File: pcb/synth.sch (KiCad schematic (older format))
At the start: 48 parts, among them J1 Conn_01x06, SW1 SW_Push, SW10 SW_Push, SW11 SW_Push, SW12 SW_Push, SW13 SW_Push, SW14 SW_Push, SW15 SW_Push, SW16 SW_Push, SW17 SW_Push, SW18 SW_Push, SW19 SW_Push, SW2 SW_Push, SW20 SW_Push, SW21 SW_Push, SW22 SW_Push, SW23 SW_Push, SW24 SW_Push, SW3 SW_Push, SW4 SW_Push, SW5 SW_Push, SW6 SW_Push, SW7 SW_Push, SW8 SW_Push, SW9 SW_Push, U1 STM32F407VGTx, Y1 Crystal

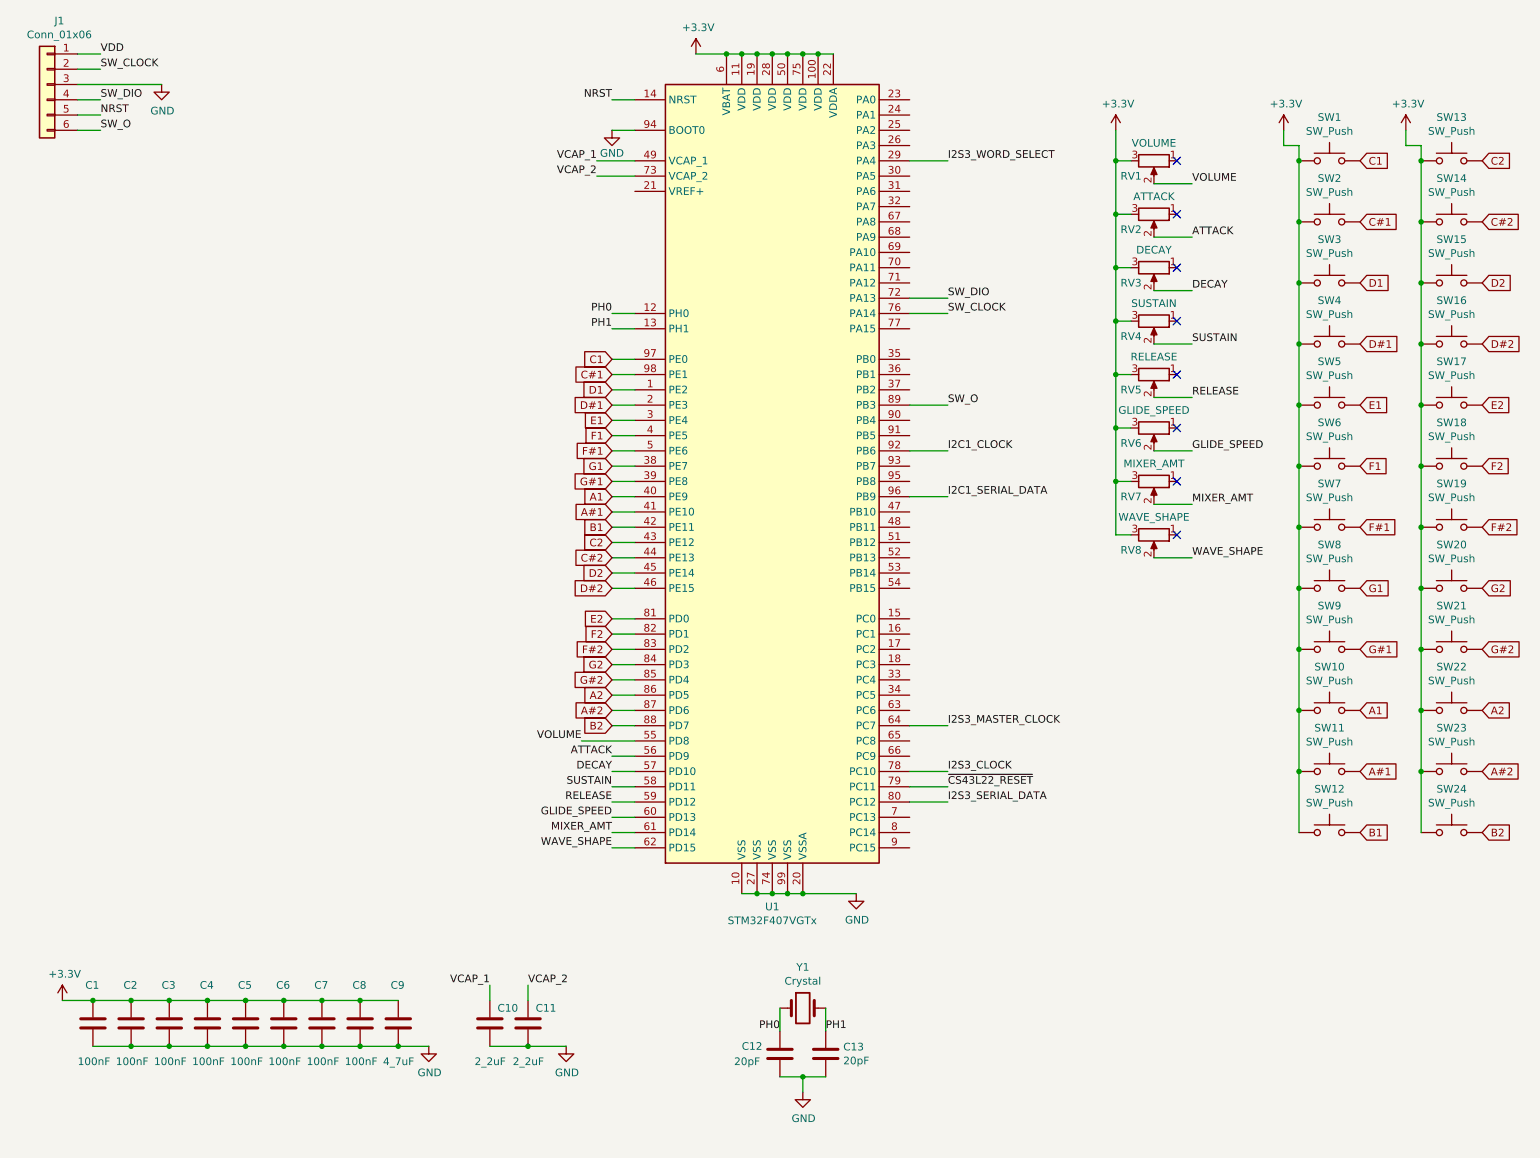
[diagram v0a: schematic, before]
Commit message: Add power flags and update the crystal to be 8 MHz.
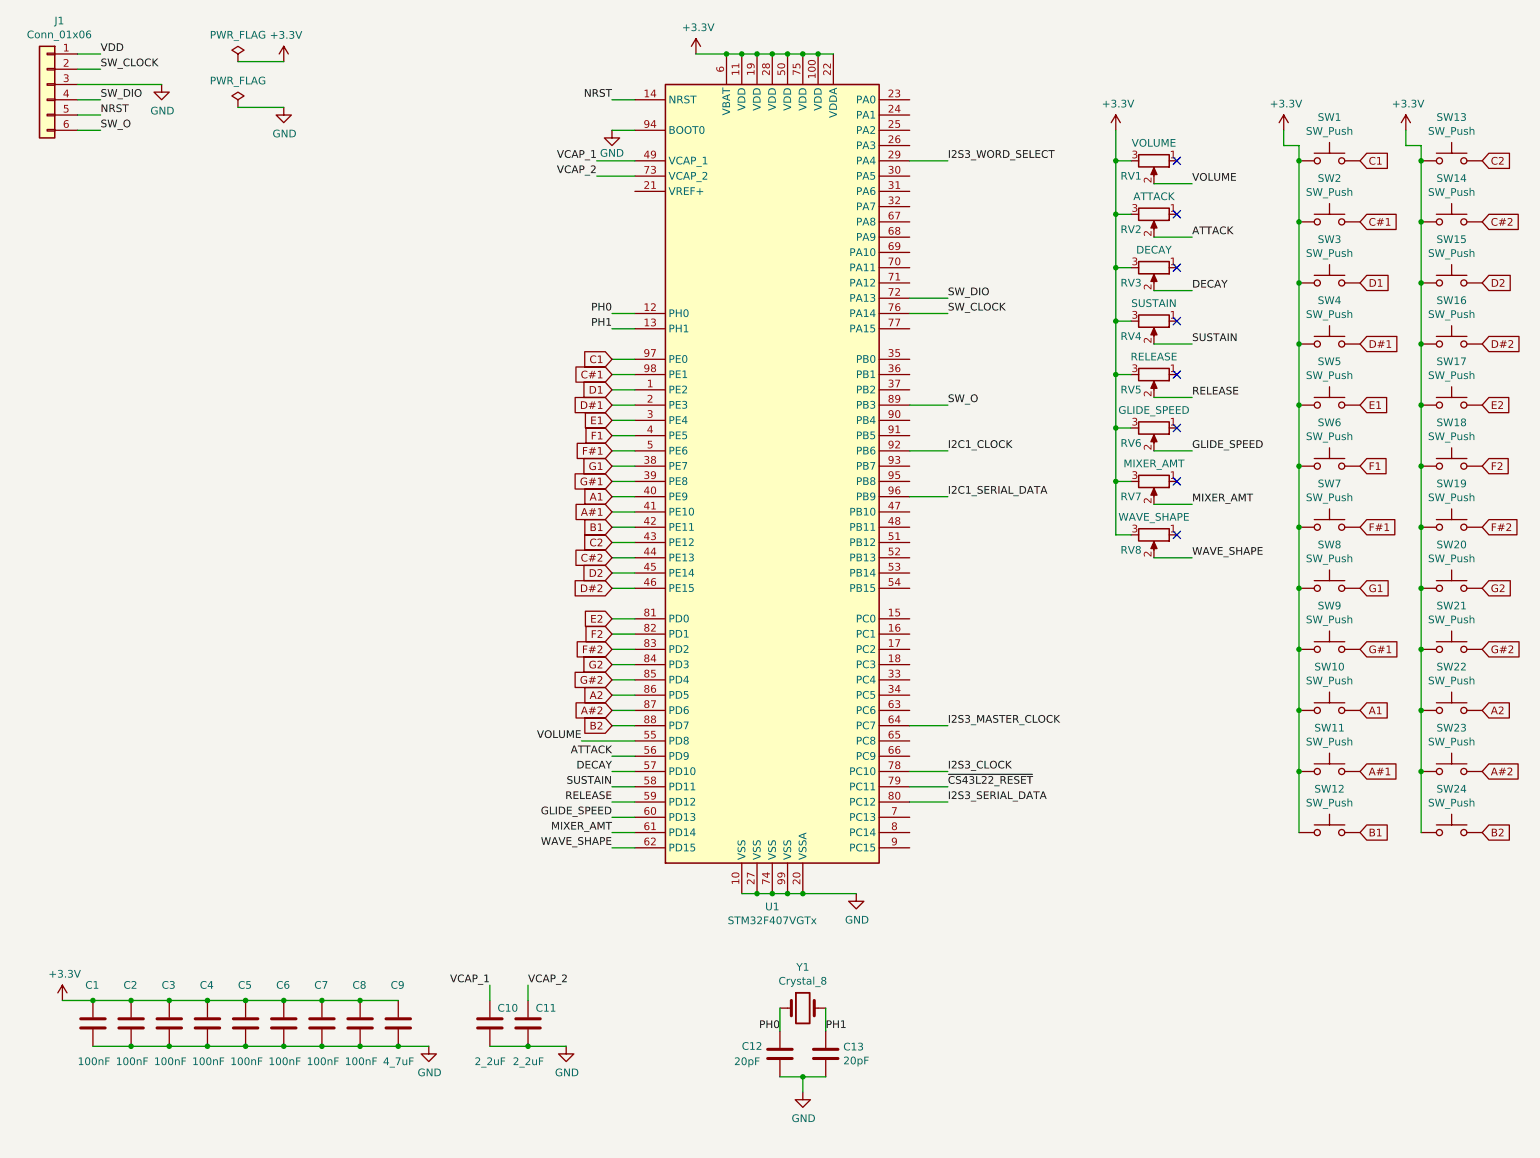
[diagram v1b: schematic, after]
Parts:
- Y1: value Crystal -> Crystal_8
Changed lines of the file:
@@
 P 5650 7050
 F 0 "Y1" H 5650 7318 50  0000 C CNN
-F 1 "Crystal" H 5650 7227 50  0000 C CNN
+F 1 "Crystal_8" H 5650 7227 50  0000 C CNN
 F 2 "" H 5650 7050 50  0001 C CNN
 F 3 "~" H 5650 7050 50  0001 C CNN
@@
 Wire Wire Line
 	7950 2700 8200 2700
+$Comp
+L power:PWR_FLAG #FLG0101
+U 1 1 5C6CDE82
+P 1950 850
+F 0 "#FLG0101" H 1950 925 50  0001 C CNN
+F 1 "PWR_FLAG" H 1950 1024 50  0000 C CNN
+F 2 "" H 1950 850 50  0001 C CNN
+F 3 "~" H 1950 850 50  0001 C CNN
+	1    1950 850
+	1    0    0    -1
+$EndComp
+$Comp
+L power:PWR_FLAG #FLG0102
+U 1 1 5C6CE054
+P 1950 1150
+F 0 "#FLG0102" H 1950 1225 50  0001 C CNN
+F 1 "PWR_FLAG" H 1950 1324 50  0000 C CNN
+F 2 "" H 1950 1150 50  0001 C CNN
+F 3 "~" H 1950 1150 50  0001 C CNN
+	1    1950 1150
+	1    0    0    -1
+$EndComp
+$Comp
+L power:GND #PWR0101
+U 1 1 5C6CE106
+P 2250 1150
+F 0 "#PWR0101" H 2250 900 50  0001 C CNN
+F 1 "GND" H 2255 977 50  0000 C CNN
+F 2 "" H 2250 1150 50  0001 C CNN
+F 3 "" H 2250 1150 50  0001 C CNN
+	1    2250 1150
+	1    0    0    -1
+$EndComp
+$Comp
+L power:+3.3V #PWR0102
+U 1 1 5C6CE1BF
+P 2250 850
+F 0 "#PWR0102" H 2250 700 50  0001 C CNN
+F 1 "+3.3V" H 2265 1023 50  0000 C CNN
+F 2 "" H 2250 850 50  0001 C CNN
+F 3 "" H 2250 850 50  0001 C CNN
+	1    2250 850
+	1    0    0    -1
+$EndComp
+Wire Wire Line
+	1950 850  2250 850
+Wire Wire Line
+	1950 1150 2250 1150
 $EndSCHEMATC

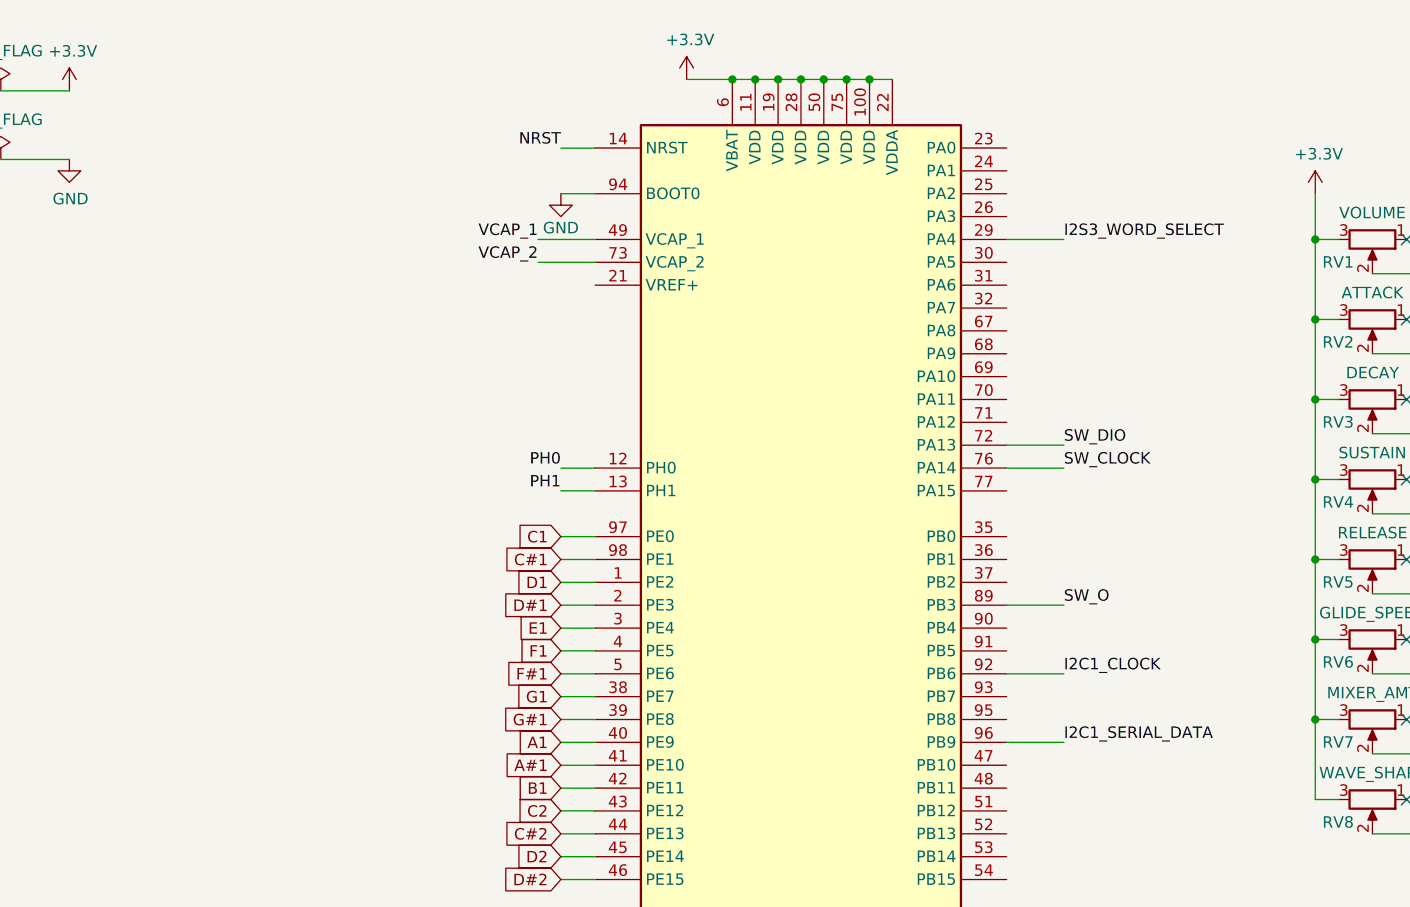
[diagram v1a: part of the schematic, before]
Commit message: Add i2c pullup resistors.
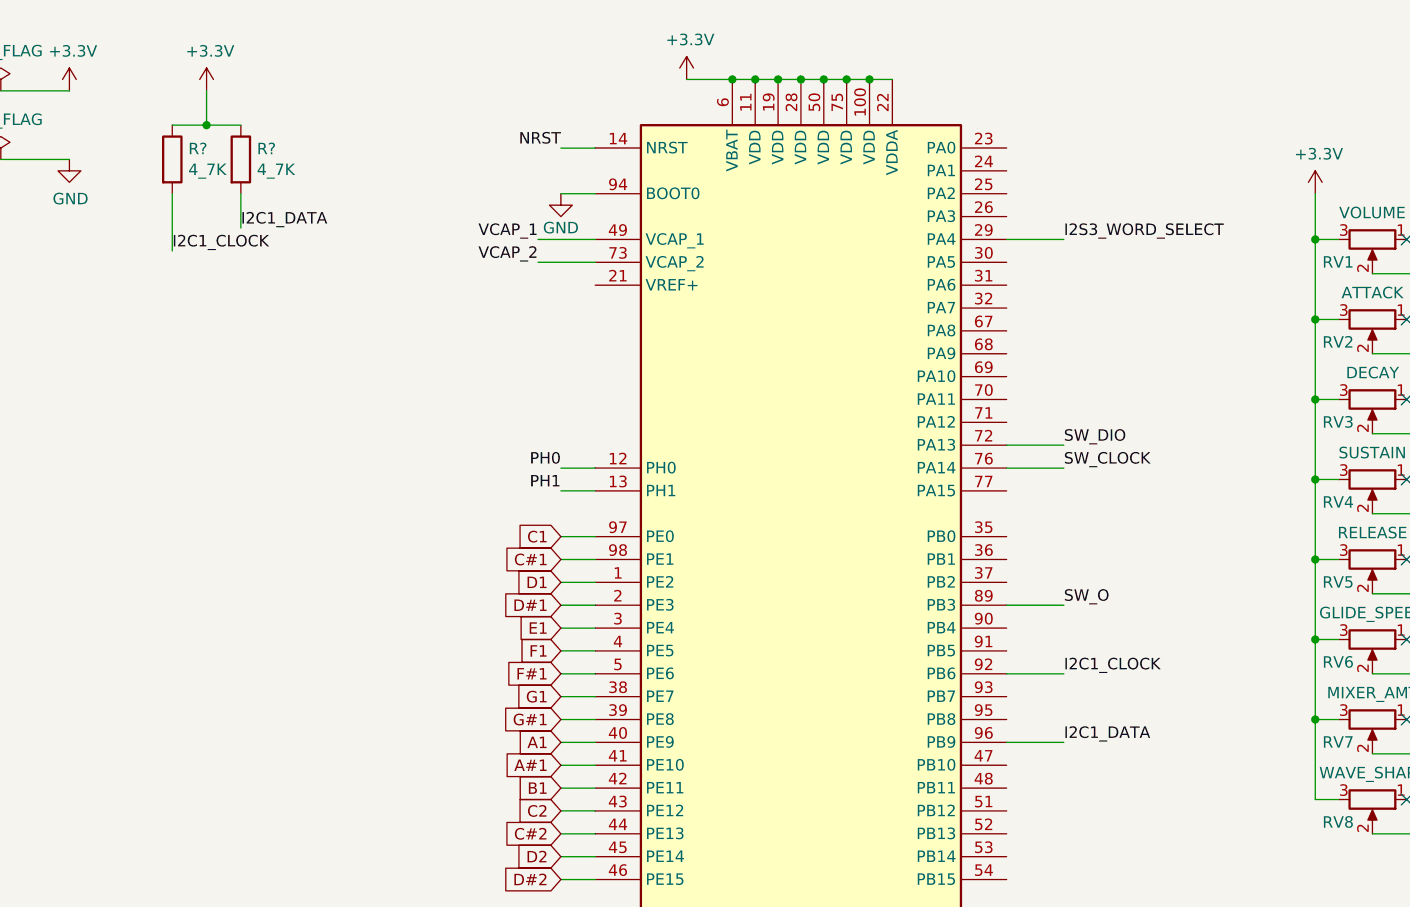
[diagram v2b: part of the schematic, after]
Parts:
- added R? (x2): 4_7K, symbol Device:R
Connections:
- net +3V3: now also R?.1, R?.1
- net I2C1_CLOCK: now also R?.2
- net I2C1_SERIAL_DATA renamed I2C1_DATA
- net I2C1_DATA: now also R?.2
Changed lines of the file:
@@
 I2C1_CLOCK
 Text Label 6600 3700 0    50   ~ 0
-I2C1_SERIAL_DATA
+I2C1_DATA
 Text Label 6600 5200 0    50   ~ 0
 I2S3_MASTER_CLOCK
@@
 Wire Wire Line
 	1950 1150 2250 1150
+$Comp
+L Device:R R?
+U 1 1 5C6DCE43
+P 2700 1150
+F 0 "R?" H 2770 1196 50  0000 L CNN
+F 1 "4_7K" H 2770 1105 50  0000 L CNN
+F 2 "" V 2630 1150 50  0001 C CNN
+F 3 "~" H 2700 1150 50  0001 C CNN
+	1    2700 1150
+	1    0    0    -1
+$EndComp
+$Comp
+L Device:R R?
+U 1 1 5C6DCF9A
+P 3000 1150
+F 0 "R?" H 3070 1196 50  0000 L CNN
+F 1 "4_7K" H 3070 1105 50  0000 L CNN
+F 2 "" V 2930 1150 50  0001 C CNN
+F 3 "~" H 3000 1150 50  0001 C CNN
+	1    3000 1150
+	1    0    0    -1
+$EndComp
+Text Label 2700 1550 0    50   ~ 0
+I2C1_CLOCK
+Text Label 3000 1450 0    50   ~ 0
+I2C1_DATA
+$Comp
+L power:+3.3V #PWR?
+U 1 1 5C6DD5EF
+P 2850 850
+F 0 "#PWR?" H 2850 700 50  0001 C CNN
+F 1 "+3.3V" H 2865 1023 50  0000 C CNN
+F 2 "" H 2850 850 50  0001 C CNN
+F 3 "" H 2850 850 50  0001 C CNN
+	1    2850 850
+	1    0    0    -1
+$EndComp
+Wire Wire Line
+	3000 1000 2850 1000
+Wire Wire Line
+	2850 1000 2850 850
+Connection ~ 2850 1000
+Wire Wire Line
+	2850 1000 2700 1000
+Wire Wire Line
+	2700 1300 2700 1550
+Wire Wire Line
+	3000 1300 3000 1450
 $EndSCHEMATC
